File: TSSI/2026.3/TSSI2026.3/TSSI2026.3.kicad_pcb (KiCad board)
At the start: 2 copper layers, 40 x 39.5 mm, 27 parts, among them J1 Conn_02x02, J2 Conn_01x02, Q1 IRLZ34N, Q2 IRLZ34N, Q3 IRLZ34N, T555 Test555, U1 LM555xN, U3 IRLZ34N

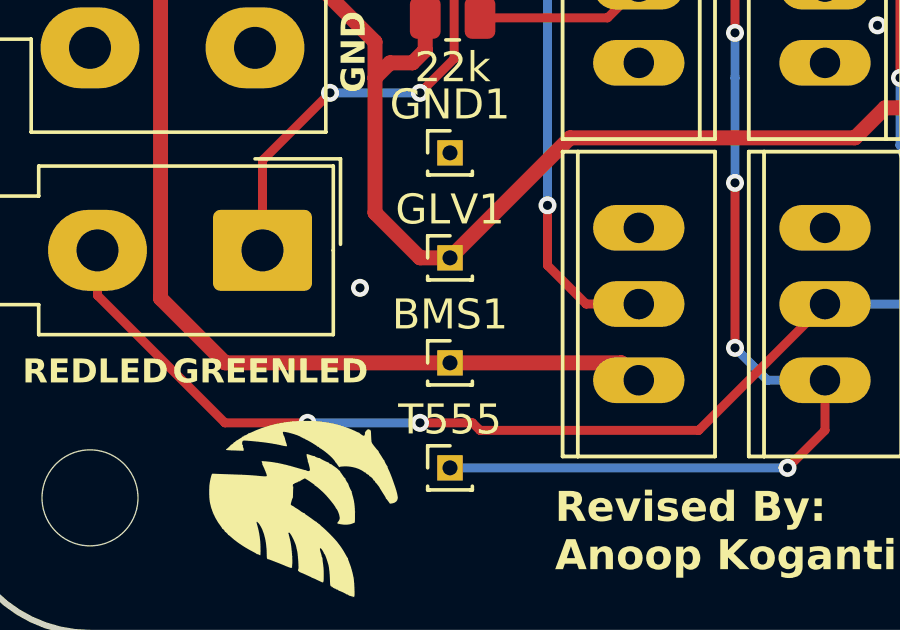
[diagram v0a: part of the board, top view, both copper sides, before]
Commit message: Redesign TSSI
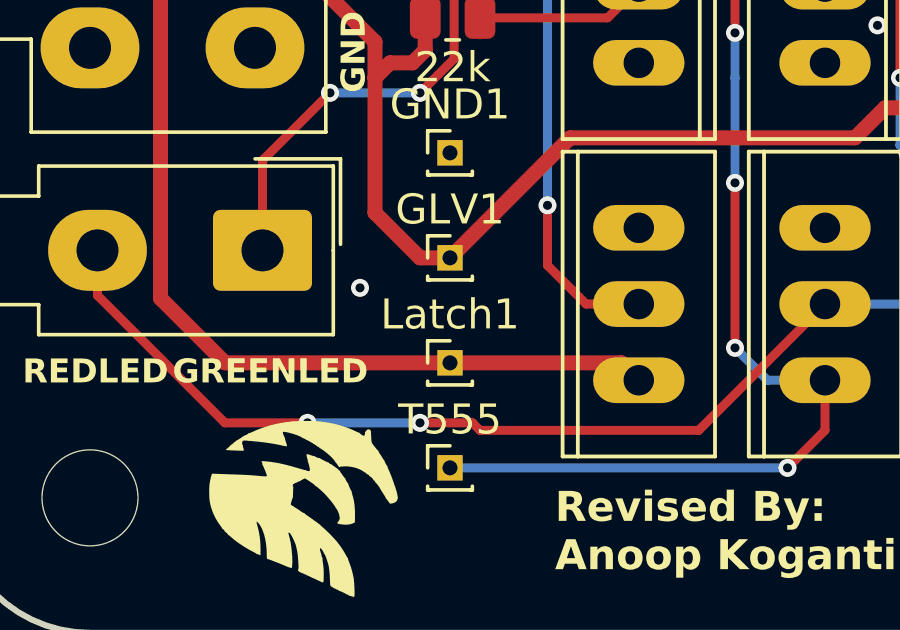
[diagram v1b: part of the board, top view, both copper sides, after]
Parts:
- renumbered BMS1 to Latch1
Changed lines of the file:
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@@
 		(descr "Through hole straight pin header, 1x01, 1.00mm pitch, single row")
 		(tags "Through hole pin header THT 1x01 1.00mm single row")
-		(property "Reference" "BMS1"
+		(property "Reference" "Latch1"
 			(at 0 -1.61 0)
 			(layer "F.SilkS")
@@
 		)
 	)
+	(dimension
+		(type orthogonal)
+		(layer "F.Fab")
+		(pts
+			(xy 39.5 60.48) (xy 79.5 61)
+		)
+		(height -7.98)
+		(orientation 0)
+		(format
+			(prefix "")
+			(suffix "")
+			(units 3)
+			(units_format 0)
+			(precision 4)
+			(suppress_zeroes yes)
+		)
+		(style
+			(thickness 0.2)
+			(arrow_length 1.27)
+			(text_position_mode 0)
+			(arrow_direction outward)
+			(extension_height 0.58642)
+			(extension_offset 0.5)
+			(keep_text_aligned yes)
+		)
+		(gr_text "40"
+			(at 59.5 50.7 0)
+			(layer "F.Fab")
+			(effects
+				(font
+					(size 1.5 1.5)
+					(thickness 0.3)
+				)
+			)
+		)
+	)
+	(dimension
+		(type orthogonal)
+		(layer "F.Fab")
+		(pts
+			(xy 73.5 53.5) (xy 73.5 93)
+		)
+		(height 9)
+		(orientation 1)
+		(format
+			(prefix "")
+			(suffix "")
+			(units 3)
+			(units_format 0)
+			(precision 4)
+			(suppress_zeroes yes)
+		)
+		(style
+			(thickness 0.2)
+			(arrow_length 1.27)
+			(text_position_mode 0)
+			(arrow_direction outward)
+			(extension_height 0.58642)
+			(extension_offset 0.5)
+			(keep_text_aligned yes)
+		)
+		(gr_text "39.5"
+			(at 80.7 73.25 90)
+			(layer "F.Fab")
+			(effects
+				(font
+					(size 1.5 1.5)
+					(thickness 0.3)
+				)
+			)
+		)
+	)

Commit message: slight Tweaks again
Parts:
- removed GLV1: TestGLV, Connector_PinHeader_1.00mm:PinHeader_1x01_P1.00mm_Vertical
- removed GND1: TestGND, Connector_PinHeader_1.00mm:PinHeader_1x01_P1.00mm_Vertical
- removed J2: Conn_01x02, Connector_Molex:Molex_Mini-Fit_Jr_5566-02A_2x01_P4.20mm_Vertical
- removed Q2: IRLZ34N, Anteater-Electric-Racing electrical-pcbs main TSSI-2026.2_KiCad_Parts_IRLZ34N:TO-220_2_
- added CCM1: TestCCMCtrl, Connector_PinHeader_1.00mm:PinHeader_1x01_P1.00mm_Vertical, F.Cu at (56.0, 80.5)
- added D2: RF01VM2S, Diode_SMD:D_0805_2012Metric, F.Cu at (73.3, 70.8)
- added D3: RF01VM2S, Diode_SMD:D_0805_2012Metric, F.Cu at (73.3, 67.5)
- added J3: Conn_02x02, Connector_Molex:Molex_Mini-Fit_Jr_5566-04A2_2x02_P4.20mm_Vertical, F.Cu at (49.5, 75.4)
- added R4: 13k, Resistor_SMD:R_0805_2012Metric, F.Cu at (56.1, 59.5)
- Latch1: value TestBMS -> TestLatch
- R1: value 10k -> 22k
- R5: value 22k -> 4k
- moved R2 25.5 mm to (69.0, 69.2), turned to 90 degrees
- moved R1 17.5 mm to (56.1, 75.8), turned to 0 degrees
- moved R5 16.2 mm to (56.1, 56.2)
- moved D1 13.1 mm to (63.0, 68.5), turned to 0 degrees
- moved C1 8.50 mm to (73.3, 74.0)
- moved C2 6.75 mm to (73.3, 77.2), turned to 0 degrees
- moved R8 5.01 mm to (73.3, 80.5)
- moved R7 4.78 mm to (56.1, 62.8)
- moved J1 4.55 mm to (49.5, 64.8)
- moved Q1 3.93 mm to (65.5, 74.0), turned to 0 degrees
- moved R6 3.03 mm to (56.0, 66.0)
- moved C3 2.59 mm to (48.8, 57.7), turned to 90 degrees
- moved U1 2.20 mm to (61.2, 63.2)
- moved R4 1.25 mm to (56.1, 69.2)
- moved G*** 0.79 mm to (50.8, 89.8)
- renumbered DebugLatch to D1
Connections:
- J1 pad 4: unconnected-(J1-Pin_4-Pad4) -> CCMCTRL
- Q1 pad GND: GREEN_LED -> Net-(D3-A)
- Q1 pad IN: Net-(Q1-PadIN) -> CCMCTRL
- Q1 pad OUT: GND -> GLV
- Q3 pad GND: Net-(Q1-PadIN) -> GREEN_LED
- Q3 pad IN: Latch_12V_Safe -> Net-(D2-K)
- R1 pad 2: Net-(Q1-PadIN) -> GREEN_LED
- R2 pad 1: Latch_12V_Safe -> Net-(D2-K)
- R5 pad 1: GLV -> CCMSensorFeedBack
- R5 pad 2: Net-(U1-R) -> GND
- U1 pad 4: Net-(U1-R) -> GREEN_LED
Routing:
- net Latch_12V_Safe: track 37.6 -> 78.0 mm, vias 0 -> 3
- net Net-(Q1-PadIN): track 37.2 -> 0.00 mm, vias 4 -> 0
- net CCMSensorFeedBack: track 0.00 -> 32.0 mm, vias 0 -> 3
- net CCMCTRL: track 0.00 -> 29.8 mm, vias 0 -> 3
- net Net-(D2-K): track 0.00 -> 26.3 mm, vias 0 -> 3
- net Net-(U1-R): track 15.0 -> 0.00 mm
- net RED_LED: track 43.8 -> 31.3 mm, vias 5 -> 2
- net Net-(U1-THR): track 27.1 -> 39.1 mm
- net GREEN_LED: track 32.0 -> 44.0 mm
- net Net-(D3-A): track 0.00 -> 10.6 mm, vias 0 -> 1
- net GLV: track 66.4 -> 60.6 mm, vias 1 -> 4
- net Net-(U1-CV): track 17.9 -> 23.2 mm, vias 0 -> 1
- net Net-(U1-DIS): track 13.7 -> 17.0 mm
- net Net-(T555-Pin_1): track 37.1 -> 38.4 mm, vias 4 -> 3
- net Net-(D1-A): track 4.20 -> 3.58 mm
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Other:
- board text added: "CCM Feedback"
- board text added: "GREEN"
- board text added: "RED"
- board text removed: "GREENLED"
- board text removed: "REDLED"

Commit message: Swapped NMOS at bottom
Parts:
- Q1, Q3, U3: footprint Anteater-Electric-Racing electrical-pcbs main TSSI-2026.2_KiCad_Parts_IRLZ34N:TO-220_2_ -> IRLZ34N:TO-220_2_
- moved G*** 0.75 mm to (50.8, 89.0)
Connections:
- Q1 pad GND: Net-(D3-A) -> GLV
- Q1 pad OUT: GLV -> Net-(D3-A)
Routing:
- net GLV: track 60.6 -> 64.3 mm, vias 4 -> 6
- net Net-(D3-A): track 10.6 -> 9.56 mm
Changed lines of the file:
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@@
 	(net 14 "CCMSensorFeedBack")
 	(net 15 "unconnected-(J3-Pin_3-Pad3)")
-	(footprint "Anteater-Electric-Racing electrical-pcbs main TSSI-2026.2_KiCad_Parts_IRLZ34N:TO-220_2_"
+	(footprint "IRLZ34N:TO-220_2_"
 		(layer "F.Cu")
 		(at 65.5 74)
 		(property "Reference" "Q1"
-			(at 0 0 270)
+			(at 0 0 0)
 			(layer "F.Fab")
 			(effects
@@
 			(layers "*.Cu" "*.Mask")
 			(remove_unused_layers no)
-			(net 13 "Net-(D3-A)")
+			(net 5 "GLV")
 			(pintype "passive")
 			(solder_mask_margin 0.102)
@@
 		)
 		(pad "OUT" thru_hole oval
-			(at 2.5 0)
+			(at 2.54 0)
 			(size 1.524 3.048)
 			(drill 1.016)
 			(layers "*.Cu" "*.Mask")
 			(remove_unused_layers no)
-			(net 5 "GLV")
+			(net 13 "Net-(D3-A)")
 			(pintype "passive")
 			(solder_mask_margin 0.102)
 		)
 		(embedded_fonts no)
-		(model "${KIPRJMOD}/Parts/IRLZ34N/IRLZ34N.step"
-			(offset
-				(xyz 0 0.8 0)
-			)
-			(scale
-				(xyz 1 1 1)
-			)
-			(rotate
-				(xyz -90 -0 -0)
-			)
-		)
 	)
 	(footprint "Diode_SMD:D_0805_2012Metric"
@@
 		)
 	)
-	(footprint "Anteater-Electric-Racing electrical-pcbs main TSSI-2026.2_KiCad_Parts_IRLZ34N:TO-220_2_"
+	(footprint "IRLZ34N:TO-220_2_"
 		(layer "F.Cu")
 		(at 68.5 82.04 90)
@@
 		)
 		(embedded_fonts no)
-		(model "${KIPRJMOD}/Parts/IRLZ34N/IRLZ34N.step"
-			(offset
-				(xyz 0 0.8 0)
-			)
-			(scale
-				(xyz 1 1 1)
-			)
-			(rotate
-				(xyz -90 -0 -0)
-			)
-		)
 	)
 	(footprint "Resistor_SMD:R_0805_2012Metric"
@@
 	(footprint "LOGO"
 		(layer "F.Cu")
-		(at 50.75 89.75)
+		(at 50.75 89)
 		(property "Reference" "G***"
 			(at 0 0 0)
@@
 		)
 	)
-	(footprint "Anteater-Electric-Racing electrical-pcbs main TSSI-2026.2_KiCad_Parts_IRLZ34N:TO-220_2_"
+	(footprint "IRLZ34N:TO-220_2_"
 		(layer "F.Cu")
 		(at 62.293 82.04 90)
@@
 		)
 		(embedded_fonts no)
-		(model "${KIPRJMOD}/Parts/IRLZ34N/IRLZ34N.step"
-			(offset
-				(xyz 0 0.8 0)
-			)
-			(scale
-				(xyz 1 1 1)
-			)
-			(rotate
-				(xyz -90 -0 -0)
-			)
-		)
 	)
 	(footprint "MountingHole:MountingHole_3.2mm_M3"
@@
 	)
 	(segment
+		(start 69.75 75.25)
+		(end 68 77)
+		(width 0.5)
+		(layer "F.Cu")
+		(net 5)
+	)
+	(segment
 		(start 70.75 75)
 		(end 70.75 76.25)
@@
 	(segment
 		(start 69.75 74)
-		(end 68 74)
+		(end 69.75 75.25)
 		(width 0.5)
 		(layer "F.Cu")
@@
 	)
 	(segment
+		(start 65.5 76.5)
+		(end 65.5 74)
+		(width 0.5)
+		(layer "F.Cu")
+		(net 5)
+	)
+	(segment
 		(start 59.25 75.5)
 		(end 60.001415 75.5)
@@
 	)
 	(segment
-		(start 65.25 76.75)
-		(end 68 74)
+		(start 61.25 76.75)
+		(end 65.25 76.75)
 		(width 0.5)
 		(layer "F.Cu")
@@
 	)
 	(segment
-		(start 61.25 76.75)
-		(end 65.25 76.75)
+		(start 55.175 69.25)
+		(end 55.175 72.5)
 		(width 0.5)
 		(layer "F.Cu")
@@
 	)
 	(segment
-		(start 55.175 69.25)
-		(end 55.175 72.5)
+		(start 65.25 76.75)
+		(end 65.5 76.5)
 		(width 0.5)
 		(layer "F.Cu")
@@
 	)
 	(via
+		(at 65.5 76.5)
+		(size 0.6)
+		(drill 0.3)
+		(layers "F.Cu" "B.Cu")
+		(net 5)
+	)
+	(via
 		(at 58.75 62.710792)
 		(size 0.6)
@@
 		(net 5)
 	)
+	(via
+		(at 68 77)
+		(size 0.6)
+		(drill 0.3)
+		(layers "F.Cu" "B.Cu")
+		(net 5)
+	)
+	(segment
+		(start 66 77)
+		(end 65.5 76.5)
+		(width 0.5)
+		(layer "B.Cu")
+		(net 5)
+	)
 	(segment
 		(start 56.960792 64.5)
@@
 	)
 	(segment
+		(start 68 77)
+		(end 66 77)
+		(width 0.5)
+		(layer "B.Cu")
+		(net 5)
+	)
+	(segment
 		(start 57.75 75.75)
 		(end 58 76)
@@
 	)
 	(segment
-		(start 65.5 72.25)
-		(end 70.25 67.5)
+		(start 70.099 71.901)
+		(end 68 74)
+		(width 0.3)
+		(layer "B.Cu")
+		(net 13)
+	)
+	(segment
+		(start 70.099 67.651)
+		(end 70.099 71.901)
 		(width 0.3)
 		(layer "B.Cu")
@@
 	)
 	(segment
-		(start 65.5 74)
-		(end 65.5 72.25)
+		(start 70.25 67.5)
+		(end 70.099 67.651)
 		(width 0.3)
 		(layer "B.Cu")
